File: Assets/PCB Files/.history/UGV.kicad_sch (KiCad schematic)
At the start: 74 parts, among them J1 B2B-XH-A, J10 B2B-XH-A, J11 B2B-XH-A, J12 B2B-XH-A, J13 USB3_A, J14 B2B-XH-A, J15 Screw_Terminal_01x12, J16 Screw_Terminal_01x12, J17 Screw_Terminal_01x12, J18 Screw_Terminal_01x12, J19 XT90PW-M, J20 XT30PW-M, J21 XT30PW-M, J23 B2B-XH-A, J24 XT30PW-M, J25 XT30PW-M, J26 XT30PW-M, J30 B2B-XH-A, J32 B2B-XH-A, J33 B2B-XH-A, J34 XT30PW-M, J35 XT30PW-M, J36 B2B-XH-A, J37 XT30PW-M, J39 XT30PW-M, J4 B4B-XH-A_LF__SN_, J40 B2B-XH-A, J41 B2B-XH-A, J42 B2B-XH-A, J43 B2B-XH-A, J44 B4B-XH-A_LF__SN_, J45 B4B-XH-A_LF__SN_, J46 B4B-XH-A_LF__SN_, J47 B4B-XH-A_LF__SN_, J5 B2B-XH-A, J6 B2B-XH-A, J7 B2B-XH-A, J8 B2B-XH-A, J9 B2B-XH-A, U1 INA219AxDCN, U2 LMR33630ADDA, U3 SN74LVC8T245, U4 Teensy4.1, U5 SN74LVC8T245

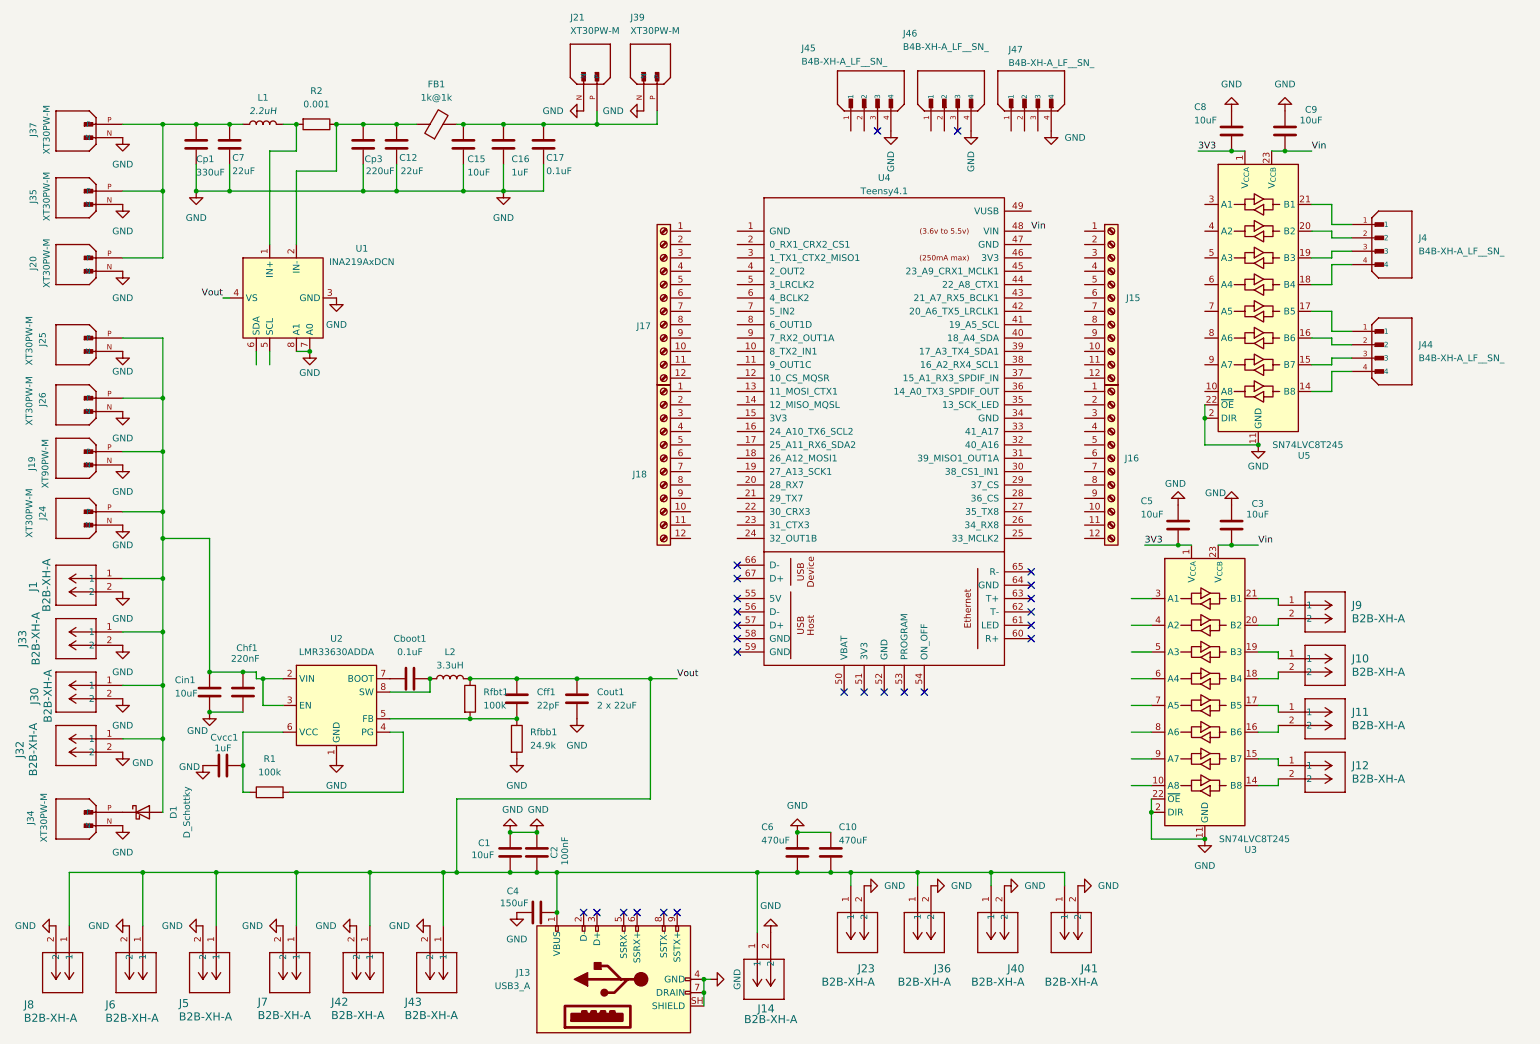
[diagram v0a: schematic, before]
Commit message: Changed the footprint
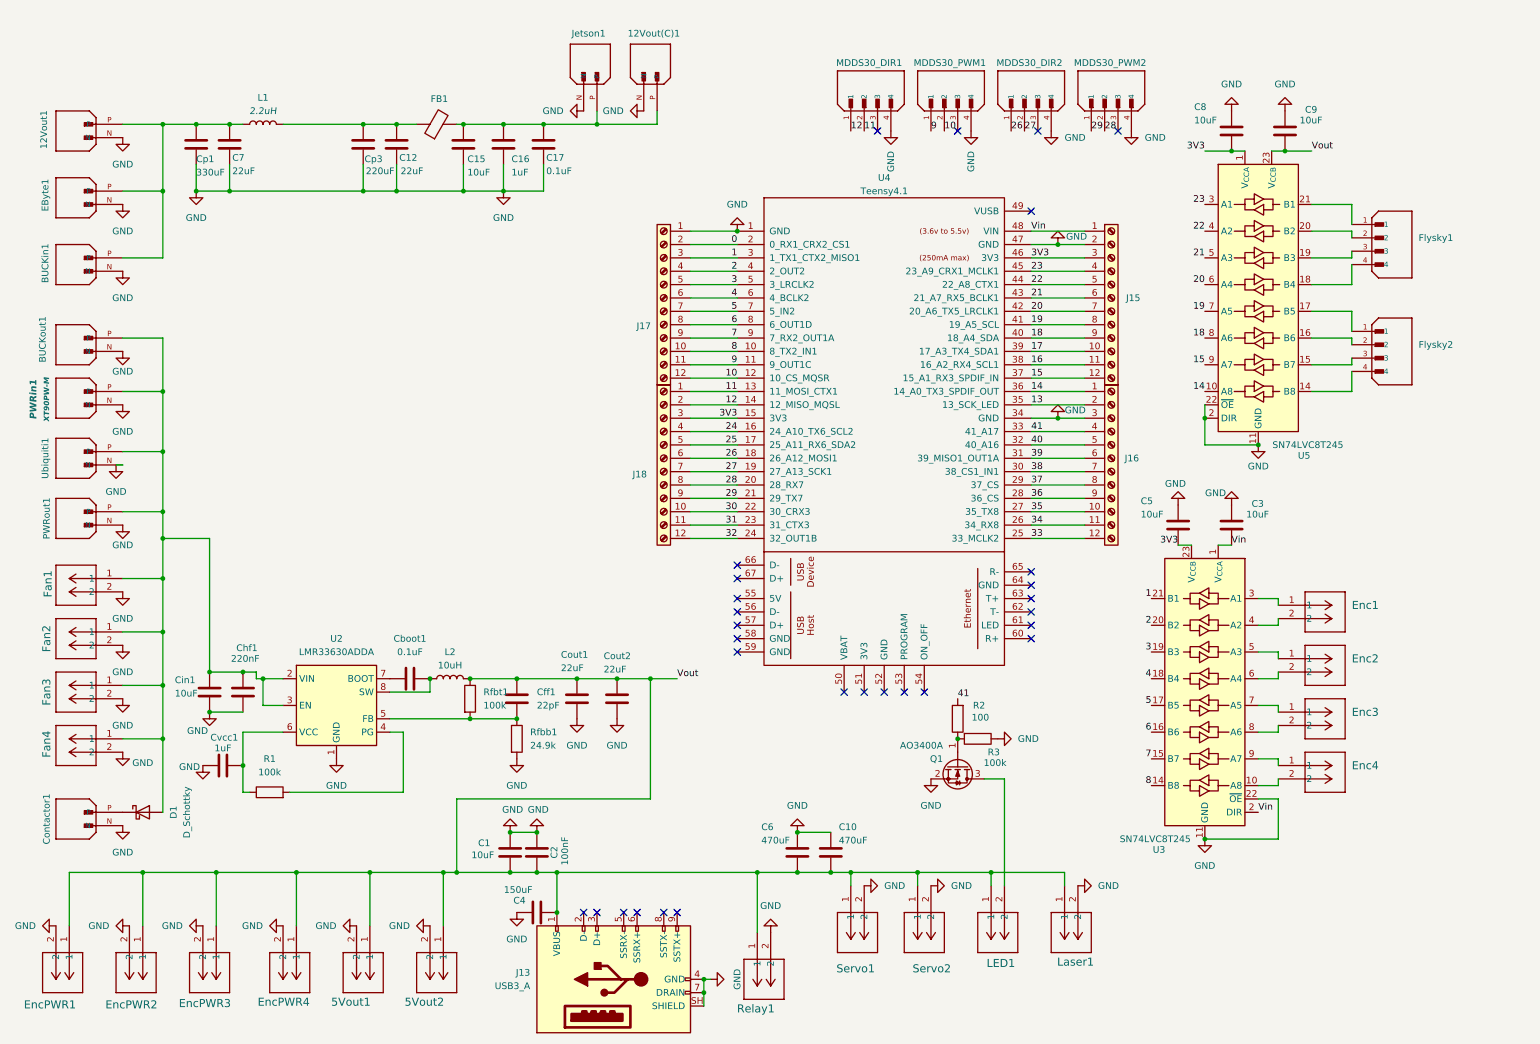
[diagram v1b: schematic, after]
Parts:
- removed U1: INA219AxDCN, Package_TO_SOT_SMD:SOT-23-8, symbol Sensor_Energy:INA219AxDCN
- added Cout2: 22uF, Capacitor_SMD:C_1210_3225Metric_Pad1.33x2.70mm_HandSolder, symbol Device:C
- added MDDS30_PWM2: B4B-XH-A_LF__SN_, Connector_JST:JST_XH_B4B-XH-A_1x04_P2.50mm_Vertical, symbol B4B-XH-A_LF__SN_:B4B-XH-A_LF__SN_
- added Q1: AO3400A, Package_TO_SOT_SMD:SOT-23, symbol Transistor_FET:AO3400A
- added R3: 100k, Resistor_SMD:R_1206_3216Metric_Pad1.30x1.75mm_HandSolder, symbol Device:R
- 12Vout(C)1: renamed from J39; footprint XT30PW-M (1):AMASS_XT30PW-M -> UGV_Custom:AMASS_XT30PW-M; MP XT30PW-M -> (none); MPN (none) -> XT30PW-M
- 12Vout1: renamed from J37; footprint XT30PW-M (1):AMASS_XT30PW-M -> UGV_Custom:AMASS_XT30PW-M; MP XT30PW-M -> (none); MPN (none) -> XT30PW-M
- 5Vout1: renamed from J42; MPN (none) -> B2B-XH-A
- 5Vout2: renamed from J43; MPN (none) -> B2B-XH-A
- BUCKin1: renamed from J20; footprint XT30PW-M (1):AMASS_XT30PW-M -> UGV_Custom:AMASS_XT30PW-M; MP XT30PW-M -> (none); MPN (none) -> XT30PW-M
- BUCKout1: renamed from J25; footprint XT30PW-M (1):AMASS_XT30PW-M -> UGV_Custom:AMASS_XT30PW-M; MP XT30PW-M -> (none); MPN (none) -> XT30PW-M
- C1, C15, C3, C5, C8, C9, Cin1: footprint Capacitor_SMD:C_1210_3225Metric -> Capacitor_SMD:C_1210_3225Metric_Pad1.33x2.70mm_HandSolder
- C12, C7: footprint Capacitor_SMD:C_1210_3225Metric -> Capacitor_SMD:C_1210_3225Metric_Pad1.33x2.70mm_HandSolder; MPN (none) -> C1210C226K3RACTU
- C16, C17, C2, Cboot1, Cvcc1: footprint Capacitor_SMD:C_0603_1608Metric -> Capacitor_SMD:C_1206_3216Metric_Pad1.33x1.80mm_HandSolder
- Cff1: footprint Capacitor_SMD:C_0603_1608Metric -> Capacitor_SMD:C_0805_2012Metric_Pad1.18x1.45mm_HandSolder
- Chf1: footprint Capacitor_SMD:C_1206_3216Metric -> Capacitor_SMD:C_1206_3216Metric_Pad1.33x1.80mm_HandSolder
- Contactor1: renamed from J34; footprint XT30PW-M (1):AMASS_XT30PW-M -> UGV_Custom:AMASS_XT30PW-M; MP XT30PW-M -> (none); MPN (none) -> XT30PW-M
- Cout1: value 2 x 22uF -> 22uF; MPN (none) -> C1210C226K3RACTU
- EByte1: renamed from J35; footprint XT30PW-M (1):AMASS_XT30PW-M -> UGV_Custom:AMASS_XT30PW-M; MP XT30PW-M -> (none); MPN (none) -> XT30PW-M
- Enc1: renamed from J9; value B2B-XH-A -> B2B-XH-A-BK; MPN (none) -> B2B-XH-A-BK
- Enc2: renamed from J10; value B2B-XH-A -> B2B-XH-A-BK; MPN (none) -> B2B-XH-A-BK
- Enc3: renamed from J11; value B2B-XH-A -> B2B-XH-A-BK; MPN (none) -> B2B-XH-A-BK
- Enc4: renamed from J12; value B2B-XH-A -> B2B-XH-A-BK; MPN (none) -> B2B-XH-A-BK
- EncPWR1: renamed from J8; MPN (none) -> B2B-XH-A
- EncPWR2: renamed from J6; MPN (none) -> B2B-XH-A
- EncPWR3: renamed from J5; MPN (none) -> B2B-XH-A
- EncPWR4: renamed from J7; MPN (none) -> B2B-XH-A
- FB1: footprint BLM21PG220SN1D:BEADC2012X105N -> Inductor_SMD:L_0805_2012Metric_Pad1.05x1.20mm_HandSolder
- Fan1: renamed from J1; value B2B-XH-A -> B2B-XH-A-R; MPN (none) -> B2B-XH-A-R
- Fan2: renamed from J33; value B2B-XH-A -> B2B-XH-A-R; MPN (none) -> B2B-XH-A-R
- Fan3: renamed from J30; value B2B-XH-A -> B2B-XH-A-R; MPN (none) -> B2B-XH-A-R
- Fan4: renamed from J32; value B2B-XH-A -> B2B-XH-A-R; MPN (none) -> B2B-XH-A-R
- Flysky1: renamed from J4; footprint B4B-XH-A_LF__SN_:JST_B4B-XH-A_LF__SN_ -> Connector_JST:JST_XH_B4B-XH-A_1x04_P2.50mm_Vertical; MP B4B-XH-A (LF)(SN) -> (none); MPN (none) -> B4B-XH-A (LF)(SN)
- Flysky2: renamed from J44; footprint B4B-XH-A_LF__SN_:JST_B4B-XH-A_LF__SN_ -> Connector_JST:JST_XH_B4B-XH-A_1x04_P2.50mm_Vertical; MP B4B-XH-A (LF)(SN) -> (none); MPN (none) -> B4B-XH-A (LF)(SN)
- J13: footprint EasyEDA_Lib:USB-3.0-TH_U233-091N-4BLPC17-11 -> UGV_Custom:USB-3.0-TH_U233-091N-4BLPC17-11
- Jetson1: renamed from J21; footprint XT30PW-M (1):AMASS_XT30PW-M -> UGV_Custom:AMASS_XT30PW-M; MP XT30PW-M -> (none); MPN (none) -> XT30PW-M
- L2: value 3.3uH -> 10uH; footprint Inductor_SMD:L_Vishay_IHLP-2525 -> UGV_Custom:SRR1280-101M
- LED1: renamed from J40; MPN (none) -> B2B-XH-A
- Laser1: renamed from J41; MPN (none) -> B2B-XH-A
- MDDS30_DIR1: renamed from J45; footprint B4B-XH-A_LF__SN_:JST_B4B-XH-A_LF__SN_ -> Connector_JST:JST_XH_B4B-XH-A_1x04_P2.50mm_Vertical; MP B4B-XH-A (LF)(SN) -> (none); MPN (none) -> B4B-XH-A (LF)(SN)
- MDDS30_DIR2: renamed from J47; footprint B4B-XH-A_LF__SN_:JST_B4B-XH-A_LF__SN_ -> Connector_JST:JST_XH_B4B-XH-A_1x04_P2.50mm_Vertical
- MDDS30_PWM1: renamed from J46; footprint B4B-XH-A_LF__SN_:JST_B4B-XH-A_LF__SN_ -> Connector_JST:JST_XH_B4B-XH-A_1x04_P2.50mm_Vertical; MP B4B-XH-A (LF)(SN) -> (none); MPN (none) -> B4B-XH-A (LF)(SN)
- PWRin1: renamed from J19; footprint XT90PW-M:AMASS_XT90PW-M -> Connector_AMASS:AMASS_XT90PW-M_1x02_P10.90mm_Horizontal
- PWRout1: renamed from J24; footprint XT30PW-M (1):AMASS_XT30PW-M -> UGV_Custom:AMASS_XT30PW-M; MP XT30PW-M -> (none); MPN (none) -> XT30PW-M
- R1, Rfbb1, Rfbt1: footprint Resistor_SMD:R_0402_1005Metric -> Resistor_SMD:R_1206_3216Metric_Pad1.30x1.75mm_HandSolder
- R2: value 0.001 -> 100; footprint Resistor_SMD:R_0402_1005Metric -> Resistor_SMD:R_0805_2012Metric_Pad1.20x1.40mm_HandSolder
- Relay1: renamed from J14; MPN (none) -> B2B-XH-A
- Servo1: renamed from J23; MPN (none) -> B2B-XH-A
- Servo2: renamed from J36; MPN (none) -> B2B-XH-A
- U2: footprint LMR33630AQRNXTQ1:CONV_LMR33620BRNXT -> UGV_Custom:LMR33630ADDAR
- U3, U5: footprint SN74LVC8T245DWR:SOIC127P1030X265-24N -> Package_SO:SOIC-24W_7.5x15.4mm_P1.27mm
- U4: footprint teensy.pretty-master:Teensy41 -> UGV_Custom:Teensy41
- Ubiquiti1: renamed from J26; footprint XT30PW-M (1):AMASS_XT30PW-M -> UGV_Custom:AMASS_XT30PW-M; MP XT30PW-M -> (none); MPN (none) -> XT30PW-M
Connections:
- net 3V3: now also J15.3 (Pin_3), J18.3 (Pin_3), U3.23 (V_{CCB}), U3.24 (V_{CCB}), U4.15 (3V3), U4.46 (3V3); no longer U3.1 (V_{CCA})
- net GND: now also C4.2, J15.2 (Pin_2), J16.3 (Pin_3), J17.1 (Pin_1), U4.1 (GND), U4.34 (GND), U4.47 (GND), Cout2.2, MDDS30_PWM2.4, Q1.2 (S), R3.1; no longer C4.1, LED1.2, U3.2 (DIR)
- net Vin: now also J15.1 (Pin_1), U3.1 (V_{CCA}), U3.2 (DIR); no longer C9.2, U3.23 (V_{CCB}), U3.24 (V_{CCB}), U5.23 (V_{CCB}), U5.24 (V_{CCB})
- net Vout: now also C4.1, C9.2, U5.23 (V_{CCB}), U5.24 (V_{CCB}), Cout2.1; no longer C4.2
- net at L1.2: now also C12.1, Cp3.1, FB1.1; no longer R2.2
- net 14: now reaches U5.10 (A8)
- net 14: now also J16.1 (Pin_1), U4.36 (14_A0_TX3_SPDIF_OUT)
- net 23: now reaches U5.3 (A1)
- net 23: now also J15.4 (Pin_4), U4.45 (23_A9_CRX1_MCLK1)
- net 22: now reaches U5.4 (A2)
- net 22: now also J15.5 (Pin_5), U4.44 (22_A8_CTX1)
- net 21: now reaches U5.5 (A3)
- net 21: now also J15.6 (Pin_6), U4.43 (21_A7_RX5_BCLK1)
- net 20: now reaches U5.6 (A4)
- net 20: now also J15.7 (Pin_7), U4.42 (20_A6_TX5_LRCLK1)
- net 19: now reaches U5.7 (A5)
- net 19: now also J15.8 (Pin_8), U4.41 (19_A5_SCL)
- net 18: now reaches U5.8 (A6)
- net 18: now also J15.9 (Pin_9), U4.40 (18_A4_SDA)
- net 15: now reaches U5.9 (A7)
- net 15: now also J15.12 (Pin_12), U4.37 (15_A1_RX3_SPDIF_IN)
- net at U3.10 (A8): now also Enc4.2
- net 8: now reaches U3.14 (B8)
- net 8: now also J17.10 (Pin_10), U4.10 (8_TX2_IN1); no longer Enc4.2
- net at Enc4.1: now also U3.9 (A7); no longer U3.15 (B7)
- net at Enc3.2: now also U3.8 (A6); no longer U3.16 (B6)
- net at Enc3.1: now also U3.7 (A5); no longer U3.17 (B5)
- net at Enc2.2: now also U3.6 (A4); no longer U3.18 (B4)
- net at Enc2.1: now also U3.5 (A3); no longer U3.19 (B3)
- net at Enc1.2: now also U3.4 (A2); no longer U3.20 (B2)
- net at Enc1.1: now also U3.3 (A1); no longer U3.21 (B1)
- net 11: now reaches J18.1 (Pin_1)
- net 11: now also MDDS30_DIR1.2, U4.13 (11_MOSI_CTX1)
- net 30: now reaches J18.10 (Pin_10)
- net 30: now also U4.22 (30_CRX3)
- net 31: now reaches J18.11 (Pin_11)
- net 31: now also U4.23 (31_CTX3)
- net 32: now reaches J18.12 (Pin_12)
- net 32: now also U4.24 (32_OUT1B)
- net 12: now reaches J18.2 (Pin_2)
- net 12: now also MDDS30_DIR1.1, U4.14 (12_MISO_MQSL)
- net 24: now reaches J18.4 (Pin_4)
- net 24: now also U4.16 (24_A10_TX6_SCL2)
- net 25: now reaches J18.5 (Pin_5)
- net 25: now also U4.17 (25_A11_RX6_SDA2)
- net 26: now reaches J18.6 (Pin_6)
- net 26: now also MDDS30_DIR2.1, U4.18 (26_A12_MOSI1)
- net 27: now reaches J18.7 (Pin_7)
- net 27: now also MDDS30_DIR2.2, U4.19 (27_A13_SCK1)
- net 28: now reaches J18.8 (Pin_8)
- net 28: now also U4.20 (28_RX7), MDDS30_PWM2.2
- net 29: now reaches J18.9 (Pin_9)
- net 29: now also U4.21 (29_TX7), MDDS30_PWM2.1
- net 17: now reaches J15.10 (Pin_10)
- net 17: now also U4.39 (17_A3_TX4_SDA1)
- net 16: now reaches J15.11 (Pin_11)
- net 16: now also U4.38 (16_A2_RX4_SCL1)
- net 9: now reaches MDDS30_PWM1.1
- net 9: now also J17.11 (Pin_11), U4.11 (9_OUT1C)
- net 10: now reaches MDDS30_PWM1.2
- net 10: now also J17.12 (Pin_12), U4.12 (10_CS_MQSR)
- net 35: now reaches J16.10 (Pin_10)
- net 35: now also U4.27 (35_TX8)
- net 34: now reaches J16.11 (Pin_11)
- net 34: now also U4.26 (34_RX8)
- net 33: now reaches J16.12 (Pin_12)
- net 33: now also U4.25 (33_MCLK2)
- net 13: now reaches J16.2 (Pin_2)
- net 13: now also U4.35 (13_SCK_LED)
- net 41: now reaches J16.4 (Pin_4)
- net 41: now also R2.2, U4.33 (41_A17)
- net 40: now reaches J16.5 (Pin_5)
- net 40: now also U4.32 (40_A16)
- net 39: now reaches J16.6 (Pin_6)
- net 39: now also U4.31 (39_MISO1_OUT1A)
- net 38: now reaches J16.7 (Pin_7)
- net 38: now also U4.30 (38_CS1_IN1)
- net 37: now reaches J16.8 (Pin_8)
- net 37: now also U4.29 (37_CS)
- net 36: now reaches J16.9 (Pin_9)
- net 36: now also U4.28 (36_CS)
- net 0: now reaches J17.2 (Pin_2)
- net 0: now also U4.2 (0_RX1_CRX2_CS1)
- net 1: now reaches J17.3 (Pin_3)
- net 1: now also U3.21 (B1), U4.3 (1_TX1_CTX2_MISO1)
- net 2: now reaches J17.4 (Pin_4)
- net 2: now also U3.20 (B2), U4.4 (2_OUT2)
- net 3: now reaches J17.5 (Pin_5)
- net 3: now also U3.19 (B3), U4.5 (3_LRCLK2)
- net 4: now reaches J17.6 (Pin_6)
- net 4: now also U3.18 (B4), U4.6 (4_BCLK2)
- net 5: now reaches J17.7 (Pin_7)
- net 5: now also U3.17 (B5), U4.7 (5_IN2)
- net 6: now reaches J17.8 (Pin_8)
- net 6: now also U3.16 (B6), U4.8 (6_OUT1D)
- net 7: now reaches J17.9 (Pin_9)
- net 7: now also U3.15 (B7), U4.9 (7_RX2_OUT1A)
- new net: Q1.1 (G), R2.1, R3.2
- new net: LED1.2, Q1.3 (D)
- no-connect marks 26 -> 29
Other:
- moved on the sheet: C4, PWRin1, Ubiquiti1
